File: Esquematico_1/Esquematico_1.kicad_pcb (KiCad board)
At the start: 6 copper layers, 40.7 x 40.7 mm, 93 parts, among them IC1 AP2112K-3.3TRG1, J1 Screw_Terminal_01x04, J2 Screw_Terminal_01x03, J3 Screw_Terminal_01x06, J4 Screw_Terminal_01x08, J5 SWD, J6 Screw_Terminal_01x04, J7 USB_C_Receptacle_USB2.0_16P, J8 Screw_Terminal_01x02, U1 ICM-42688-P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

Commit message: Update arreglo de errores
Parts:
- added J9: Screw_Terminal_01x01, TestPoint:TestPoint_Pad_2.5x2.5mm, B.Cu at (125.4, 95.5)
- J8: value Screw_Terminal_01x02 -> Screw_Terminal_01x01; footprint TerminalBlock:TerminalBlock_Xinya_XY308-2.54-2P_1x02_P2.54mm_Horizontal -> TestPoint:TestPoint_Pad_2.5x2.5mm
- moved J8 30.4 mm to (125.4, 100.4), turned to 180 degrees
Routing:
- net VCC: track 61.5 -> 79.3 mm, vias 2 -> 4

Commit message: Update pcb 0 errores
8========D
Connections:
- J7 pad A4: Net-(D3-A) -> (no net)
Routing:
- net USB_D+: track 0.00 -> 6.88 mm
- net USB_D-: track 0.00 -> 6.48 mm
- net Net-(J7-D+-PadA6): track 0.00 -> 5.48 mm
- net Net-(J7-D--PadA7): track 0.00 -> 4.97 mm
- net GND: track 58.6 -> 60.2 mm
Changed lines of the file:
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@@
 	(generator_version "9.0")
 	(general
-		(thickness 1.6)
+		(thickness 2.453)
 		(legacy_teardrops no)
 	)
@@
 			(layer "dielectric 1"
 				(type "prepreg")
-				(thickness 0.1)
-				(material "FR4")
-				(epsilon_r 4.5)
-				(loss_tangent 0.02)
+				(color "FR4 natural")
+				(thickness 0.994)
+				(material "3313 RC57% 4.2mil")
+				(epsilon_r 1)
+				(loss_tangent 0)
 			)
 			(layer "In1.Cu"
 				(type "copper")
-				(thickness 0.035)
+				(thickness 0.0152)
 			)
 			(layer "dielectric 2"
 				(type "core")
-				(thickness 0.535)
-				(material "FR4")
+				(thickness 0.55)
+				(material "0.55mm H/Hwithout copper")
 				(epsilon_r 4.5)
 				(loss_tangent 0.02)
@@
 			(layer "In2.Cu"
 				(type "copper")
-				(thickness 0.035)
+				(thickness 0.0152)
 			)
 			(layer "dielectric 3"
 				(type "prepreg")
-				(thickness 0.1)
-				(material "FR4")
+				(thickness 0.1088)
+				(material "2116 RC54% 4.9mil")
 				(epsilon_r 4.5)
 				(loss_tangent 0.02)
@@
 			(layer "In3.Cu"
 				(type "copper")
-				(thickness 0.035)
+				(thickness 0.0152)
 			)
 			(layer "dielectric 4"
 				(type "core")
-				(thickness 0.535)
-				(material "FR4")
+				(thickness 0.55)
+				(material "0.55mm H/Hwithout copper")
 				(epsilon_r 4.5)
 				(loss_tangent 0.02)
@@
 			(layer "In4.Cu"
 				(type "copper")
-				(thickness 0.035)
+				(thickness 0.0152)
 			)
 			(layer "dielectric 5"
 				(type "prepreg")
-				(thickness 0.1)
-				(material "FR4")
-				(epsilon_r 4.5)
-				(loss_tangent 0.02)
+				(color "FR4 natural")
+				(thickness 0.0994)
+				(material "3313 RC57% 4.2mil")
+				(epsilon_r 1)
+				(loss_tangent 0)
 			)
 			(layer "B.Cu"
@@
 			)
 			(copper_finish "None")
-			(dielectric_constraints no)
+			(dielectric_constraints yes)
 		)
 		(pad_to_mask_clearance 0)
@@
 			(size 0.6 1.15)
 			(layers "F.Cu" "F.Mask" "F.Paste")
-			(net 26 "Net-(D3-A)")
 			(pinfunction "VBUS")
 			(pintype "passive")
@@
 	)
 	(via
-		(at 114.6 90)
+		(at 115.1 91.44)
 		(size 0.45)
 		(drill 0.3)
@@
 	)
 	(segment
+		(start 114.5925 90.0075)
+		(end 113.23 90.0075)
+		(width 0.2)
+		(layer "B.Cu")
+		(net 4)
+	)
+	(segment
 		(start 104.9 99.7625)
 		(end 105.15 99.5125)
@@
 	)
 	(segment
-		(start 114.5925 90.0075)
-		(end 114.6 90)
+		(start 105.426 97.351)
+		(end 106.15 96.627)
 		(width 0.2)
 		(layer "B.Cu")
@@
 	)
 	(segment
-		(start 105.426 97.351)
-		(end 106.15 96.627)
+		(start 92.15 79.28)
+		(end 93.02 79.28)
 		(width 0.2)
 		(layer "B.Cu")
@@
 	)
 	(segment
-		(start 92.15 79.28)
-		(end 93.02 79.28)
+		(start 115.1 91.44)
+		(end 115.1 90.515)
 		(width 0.2)
 		(layer "B.Cu")
@@
 	)
 	(segment
-		(start 113.23 90.0075)
+		(start 115.1 90.515)
 		(end 114.5925 90.0075)
 		(width 0.2)
@@
 	)
 	(segment
+		(start 116.2783 90.1733)
+		(end 110.1108 90.1733)
+		(width 0.2)
+		(layer "F.Cu")
+		(net 14)
+	)
+	(segment
+		(start 116.4525 90.3475)
+		(end 116.2783 90.1733)
+		(width 0.2)
+		(layer "F.Cu")
+		(net 14)
+	)
+	(segment
+		(start 110.1108 90.1733)
+		(end 110.065 90.1275)
+		(width 0.2)
+		(layer "F.Cu")
+		(net 14)
+	)
+	(segment
 		(start 110.899 95.1275)
 		(end 110.065 95.1275)
@@
 	)
 	(segment
-		(start 117.114999 89.3975)
-		(end 117.366 89.146499)
-		(width 0.2)
-		(layer "F.Cu")
-		(net 18)
-	)
-	(segment
 		(start 95.38 79.42)
 		(end 95.38 79.5625)
@@
 	)
 	(segment
-		(start 116.4525 89.3975)
-		(end 117.114999 89.3975)
-		(width 0.2)
-		(layer "F.Cu")
-		(net 18)
-	)
-	(segment
 		(start 97 79.2)
 		(end 95.6 79.2)
@@
 	)
 	(segment
-		(start 117.366 86.4735)
+		(start 117.59 86.6975)
 		(end 116.6775 85.785)
 		(width 0.2)
@@
 	)
 	(segment
+		(start 116.4525 89.3975)
+		(end 117.114999 89.3975)
+		(width 0.2)
+		(layer "F.Cu")
+		(net 18)
+	)
+	(segment
 		(start 95.6 79.2)
 		(end 95.38 79.42)
@@
 	)
 	(segment
-		(start 117.366 89.146499)
-		(end 117.366 86.4735)
+		(start 117.114999 89.3975)
+		(end 117.59 88.922499)
+		(width 0.2)
+		(layer "F.Cu")
+		(net 18)
+	)
+	(segment
+		(start 117.59 88.922499)
+		(end 117.59 86.6975)
 		(width 0.2)
 		(layer "F.Cu")
@@
 	(segment
 		(start 121.265 87.4375)
-		(end 122.156008 87.4375)
+		(end 122.6025 87.4375)
 		(width 0.2)
 		(layer "F.Cu")
@@
 	)
 	(segment
-		(start 122.156008 87.4375)
-		(end 123.141 86.452508)
+		(start 123.27 81.3075)
+		(end 122.84 80.8775)
 		(width 0.2)
 		(layer "F.Cu")
@@
 	)
 	(segment
-		(start 123.141 86.452508)
-		(end 123.141 81.1785)
+		(start 123.27 86.77)
+		(end 123.27 81.3075)
 		(width 0.2)
 		(layer "F.Cu")
@@
 	)
 	(segment
-		(start 123.141 81.1785)
-		(end 122.84 80.8775)
+		(start 122.6025 87.4375)
+		(end 123.27 86.77)
 		(width 0.2)
 		(layer "F.Cu")
@@
 	)
 	(segment
+		(start 114.224098 89.6275)
+		(end 110.065 89.6275)
+		(width 0.2)
+		(layer "F.Cu")
+		(net 53)
+	)
+	(segment
+		(start 116.4525 88.4475)
+		(end 115.404098 88.4475)
+		(width 0.2)
+		(layer "F.Cu")
+		(net 53)
+	)
+	(segment
+		(start 115.404098 88.4475)
+		(end 114.224098 89.6275)
+		(width 0.2)
+		(layer "F.Cu")
+		(net 53)
+	)
+	(segment
 		(start 110.065 90.6275)
 		(end 107.4275 90.6275)
@@
 	)
 	(segment
+		(start 119.95 89.4775)
+		(end 119.95 90.2)
+		(width 0.2)
+		(layer "F.Cu")
+		(net 62)
+	)
+	(segment
+		(start 120.49 88.9375)
+		(end 119.95 89.4775)
+		(width 0.2)
+		(layer "F.Cu")
+		(net 62)
+	)
+	(segment
+		(start 121.265 89.9375)
+		(end 120.2125 89.9375)
+		(width 0.2)
+		(layer "F.Cu")
+		(net 62)
+	)
+	(segment
+		(start 119.8025 90.3475)
+		(end 118.7275 90.3475)
+		(width 0.2)
+		(layer "F.Cu")
+		(net 62)
+	)
+	(segment
+		(start 121.265 88.9375)
+		(end 120.49 88.9375)
+		(width 0.2)
+		(layer "F.Cu")
+		(net 62)
+	)
+	(segment
+		(start 120.2125 89.9375)
+		(end 119.95 90.2)
+		(width 0.2)
+		(layer "F.Cu")
+		(net 62)
+	)
+	(segment
+		(start 119.95 90.2)
+		(end 119.8025 90.3475)
+		(width 0.2)
+		(layer "F.Cu")
+		(net 62)
+	)
+	(segment
 		(start 106.65 84.87)
 		(end 106.65 86.1925)
@@
 	)
 	(segment
+		(start 122.1825 89.4375)
+		(end 122.34 89.28)
+		(width 0.2)
+		(layer "F.Cu")
+		(net 86)
+	)
+	(segment
+		(start 122.34 88.64)
+		(end 122.1375 88.4375)
+		(width 0.2)
+		(layer "F.Cu")
+		(net 86)
+	)
+	(segment
+		(start 118.7375 88.4375)
+		(end 118.7275 88.4475)
+		(width 0.2)
+		(layer "F.Cu")
+		(net 86)
+	)
+	(segment
+		(start 121.265 88.4375)
+		(end 118.7375 88.4375)
+		(width 0.2)
+		(layer "F.Cu")
+		(net 86)
+	)
+	(segment
+		(start 122.34 89.28)
+		(end 122.34 88.64)
+		(width 0.2)
+		(layer "F.Cu")
+		(net 86)
+	)
+	(segment
+		(start 121.265 89.4375)
+		(end 122.1825 89.4375)
+		(width 0.2)
+		(layer "F.Cu")
+		(net 86)
+	)
+	(segment
+		(start 122.1375 88.4375)
+		(end 121.265 88.4375)
+		(width 0.2)
+		(layer "F.Cu")
+		(net 86)
+	)
+	(segment

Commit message: Pequeños retoques de los nombres
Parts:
- renumbered SwBoot1 to Boot, F5 to GPS, SwReset1 to Reset
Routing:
- net GND: track 60.2 -> 62.5 mm, vias 33 -> 35
- net SDIO_D1: track 6.63 -> 6.06 mm

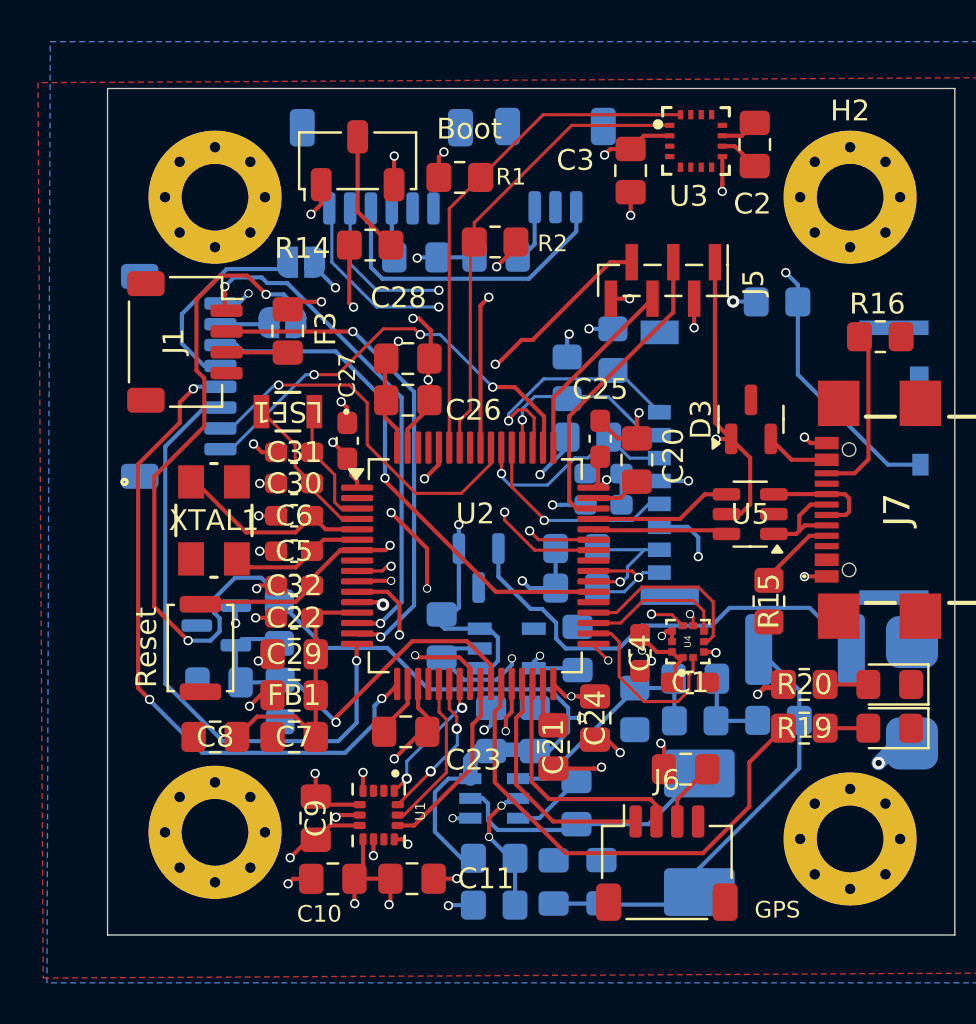
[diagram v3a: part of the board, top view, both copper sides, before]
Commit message: Add 3d model pa
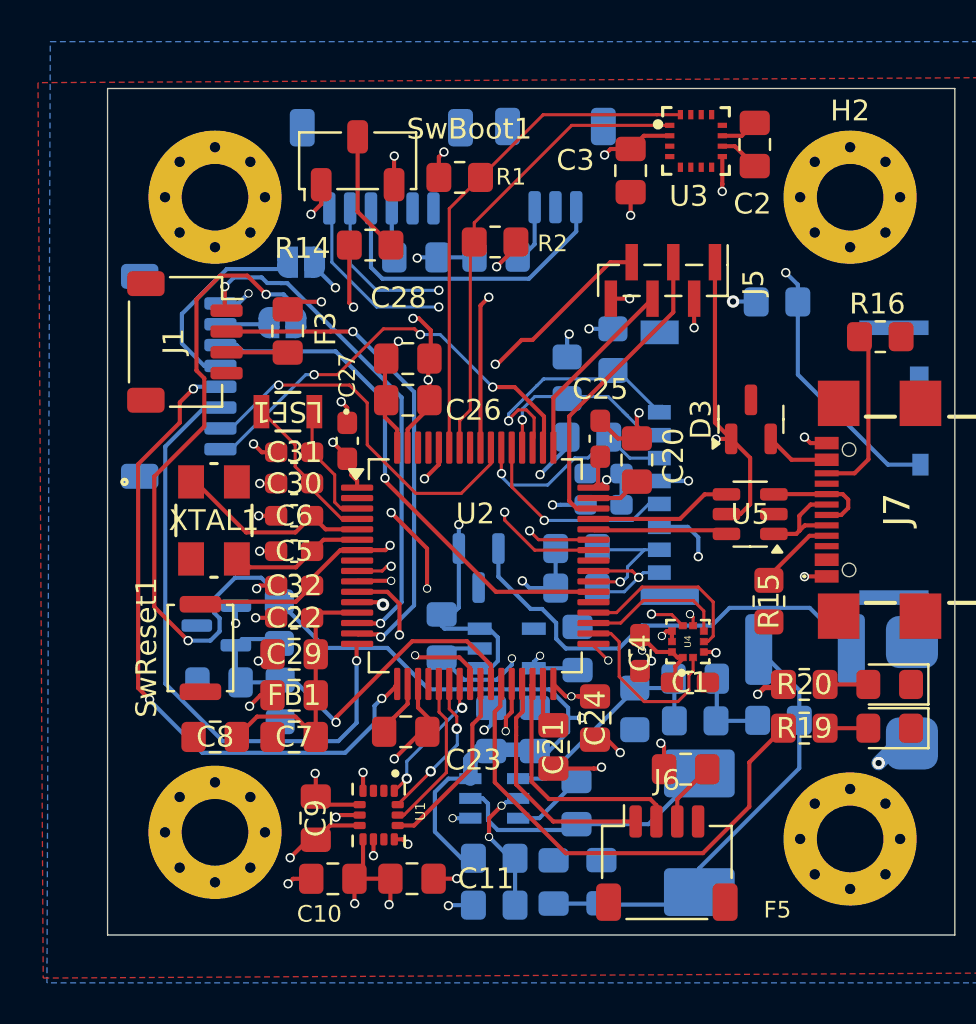
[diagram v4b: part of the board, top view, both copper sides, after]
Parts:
- renumbered GPS to F5, Boot to SwBoot1, Reset to SwReset1
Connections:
- J7 pad A4: (no net) -> Net-(D3-A)
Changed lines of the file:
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@@
 		(descr "Capacitor SMD 0805 (2012 Metric), square (rectangular) end terminal, IPC-7351 nominal with elongated pad for handsoldering. (Body size source: IPC-SM-782 page 76, https://www.pcb-3d.com/wordpress/wp-content/uploads/ipc-sm-782a_amendment_1_and_2.pdf, https://docs.google.com/spreadsheets/d/1BsfQQcO9C6DZCsRaXUlFlo91Tg2WpOkGARC1WS5S8t0/edit?usp=sharing), generated with kicad-footprint-generator")
 		(tags "capacitor handsolder")
-		(property "Reference" "GPS"
+		(property "Reference" "F5"
 			(at -4.4075 -6.7525 0)
 			(layer "F.SilkS")
@@
 				(font
 					(size 0.48 0.48)
-					(thickness 0.15)
+					(thickness 0.12)
 				)
 			)
@@
 				(font
 					(size 0.48 0.48)
-					(thickness 0.15)
+					(thickness 0.12)
 				)
 			)
@@
 		)
 		(embedded_fonts no)
+		(model "${KIPRJMOD}/Footprints/ICM_42688_P/ICM-42688-P.step"
+			(offset
+				(xyz 0 0 0)
+			)
+			(scale
+				(xyz 1 1 1)
+			)
+			(rotate
+				(xyz -90 -0 -0)
+			)
+		)
 	)
 	(footprint "Resistor_SMD:R_0805_2012Metric_Pad1.20x1.40mm_HandSolder"
@@
 		)
 		(embedded_fonts no)
+		(model "${KIPRJMOD}/Footprints/BMP388/BMP388.step"
+			(offset
+				(xyz 0 0 0)
+			)
+			(scale
+				(xyz 1 1 1)
+			)
+			(rotate
+				(xyz -90 -0 90)
+			)
+		)
 	)
 	(footprint "Button_Switch_SMD:Nidec_Copal_CAS-120A"
@@
 		(descr "Slide Switch, SMD, Nidec CAS series, https://www.nidec-components.com/e/catalog/switch/cas.pdf")
 		(tags "SMD slide switch Nidec CAS 120A ")
-		(property "Reference" "Boot"
+		(property "Reference" "SwBoot1"
 			(at 1.5275 5.36 0)
 			(unlocked yes)
@@
 			(size 0.6 1.15)
 			(layers "F.Cu" "F.Mask" "F.Paste")
+			(net 26 "Net-(D3-A)")
 			(pinfunction "VBUS")
 			(pintype "passive")
@@
 		)
 		(embedded_fonts no)
+		(model "${KIPRJMOD}/Footprints/LIB_USB4940-00-A/ul_2295018-2/c-2295018-2-b-3d.stp"
+			(offset
+				(xyz 0 -4 1.3)
+			)
+			(scale
+				(xyz 1 1 1)
+			)
+			(rotate
+				(xyz -90 -0 -0)
+			)
+		)
 	)
 	(footprint "Capacitor_SMD:C_0805_2012Metric_Pad1.18x1.45mm_HandSolder"
@@
 		(descr "http://www.alps.com/prod/info/E/HTML/Tact/SurfaceMount/SKRK/SKRKAHE020.html")
 		(tags "SMD SMT button")
-		(property "Reference" "Reset"
+		(property "Reference" "SwReset1"
 			(at 0.0275 -2.59 90)
 			(layer "F.SilkS")
@@
 		)
 		(embedded_fonts no)
+		(model "${KIPRJMOD}/Footprints/MOLEX 5033981892/ul_5033981892/5033981892.stp"
+			(offset
+				(xyz -136 -16 154.4)
+			)
+			(scale
+				(xyz 1 1 1)
+			)
+			(rotate
+				(xyz -0 -180 -180)
+			)
+		)
 	)
 	(footprint "Capacitor_SMD:C_0805_2012Metric_Pad1.18x1.45mm_HandSolder"
@@
 	)
 	(segment
-		(start 122.1825 89.4375)
-		(end 122.34 89.28)
+		(start 122.3 88.7)
+		(end 122.0375 88.4375)
 		(width 0.2)
 		(layer "F.Cu")
@@
 	)
 	(segment
-		(start 122.34 88.64)
-		(end 122.1375 88.4375)
+		(start 118.7375 88.4375)
+		(end 118.7275 88.4475)
 		(width 0.2)
 		(layer "F.Cu")
@@
 	)
 	(segment
-		(start 118.7375 88.4375)
-		(end 118.7275 88.4475)
+		(start 121.265 89.4375)
+		(end 121.9625 89.4375)
 		(width 0.2)
 		(layer "F.Cu")
@@
 	)
 	(segment
-		(start 121.265 88.4375)
-		(end 118.7375 88.4375)
+		(start 121.9625 89.4375)
+		(end 122.3 89.1)
 		(width 0.2)
 		(layer "F.Cu")
@@
 	)
 	(segment
-		(start 122.34 89.28)
-		(end 122.34 88.64)
+		(start 122.3 89.1)
+		(end 122.3 88.7)
 		(width 0.2)
 		(layer "F.Cu")
@@
 	)
 	(segment
-		(start 121.265 89.4375)
-		(end 122.1825 89.4375)
+		(start 121.265 88.4375)
+		(end 118.7375 88.4375)
 		(width 0.2)
 		(layer "F.Cu")
@@
 	)
 	(segment
-		(start 122.1375 88.4375)
+		(start 122.0375 88.4375)
 		(end 121.265 88.4375)
 		(width 0.2)

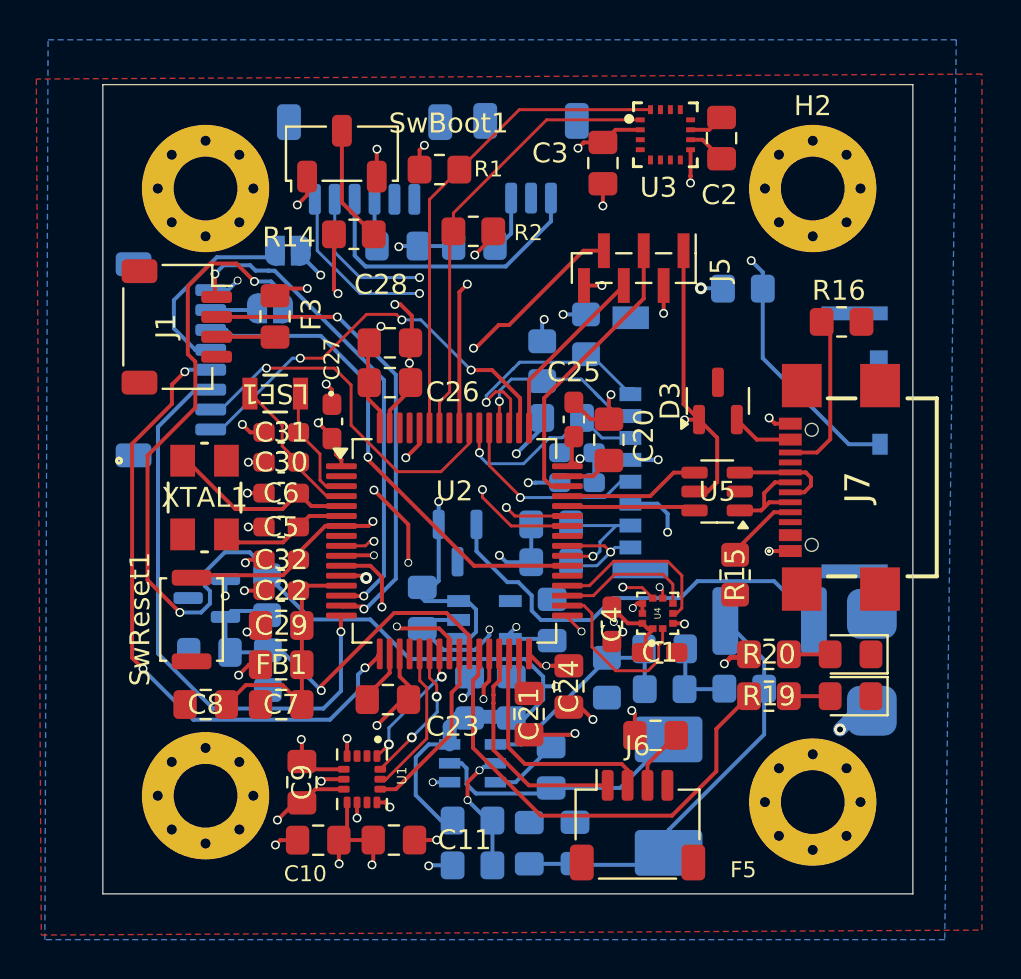
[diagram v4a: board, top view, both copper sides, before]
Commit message: Cambio de la SD, re ruteo del ESC para mayor fiabilidad, correción en el clearence
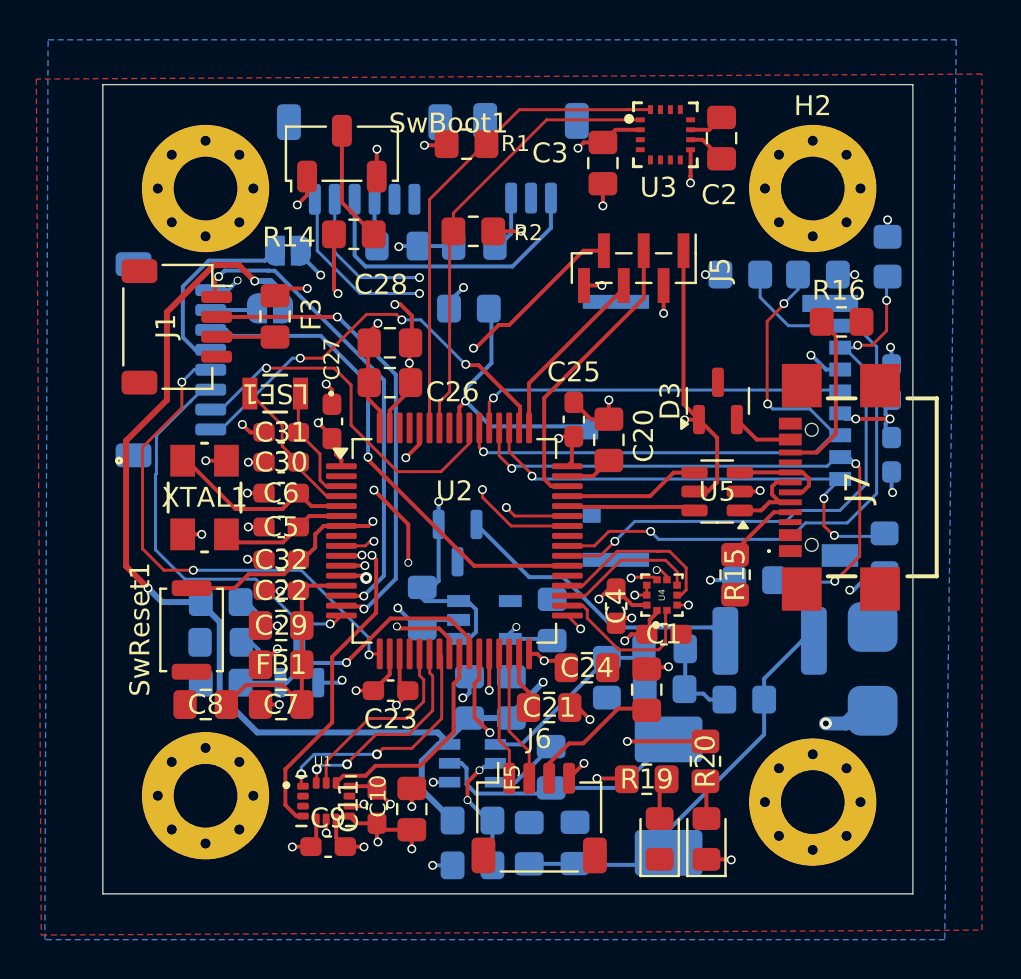
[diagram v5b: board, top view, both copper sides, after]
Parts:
- C11, C23, C9: footprint Capacitor_SMD:C_0805_2012Metric_Pad1.18x1.45mm_HandSolder -> Capacitor_SMD:C_0603_1608Metric_Pad1.08x0.95mm_HandSolder
- moved R7 21.6 mm to (126.2, 77.6), turned to -90 degrees
- moved R4 18.6 mm to (126.0, 92.5), turned to 90 degrees
- moved R8 17.3 mm to (118.8, 78.5)
- moved C34 16.6 mm to (126.3, 83.9), turned to -90 degrees
- moved C35 15.8 mm to (126.3, 87.5), turned to 90 degrees
- moved R5 15.3 mm to (119.5, 93.8), turned to 0 degrees
- moved R6 14.7 mm to (122.7, 78.5), turned to 180 degrees
- moved R3 13.8 mm to (105.1, 80.2)
- moved D8 12.0 mm to (114.7, 106.8), turned to 90 degrees
- moved D7 11.8 mm to (117.0, 106.8), turned to 90 degrees
- moved R19 7.42 mm to (114.0, 103.8)
- moved R20 6.25 mm to (117.0, 103.0), turned to -90 degrees
- moved D1 5.71 mm to (96.6, 98.1), turned to 90 degrees
- moved J6 4.95 mm to (108.7, 105.8)
- moved C10 4.95 mm to (102.2, 105.3), turned to 90 degrees
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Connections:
- J7 pad A4: Net-(D3-A) -> (no net)
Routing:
- net SDIO_D1: track 6.06 -> 32.4 mm
- net SDIO_D0: track 6.38 -> 29.4 mm, vias 1 -> 3
- net CardDetect: track 35.0 -> 13.6 mm, vias 2 -> 1
- net SDIO_CMD: track 10.5 -> 31.0 mm, vias 1 -> 3
- net SDIO_D3: track 9.79 -> 29.6 mm, vias 1 -> 3
- net SDIO_D2: track 12.2 -> 24.5 mm, vias 1 -> 3
- net /MCU/LRed: track 23.9 -> 12.2 mm, vias 0 -> 2
- net SDIO_CLK: track 10.0 -> 19.2 mm
- net ESC3: track 29.3 -> 20.5 mm
- net ESC4: track 32.5 -> 25.5 mm
- net Net-(D4-A): track 21.8 -> 15.7 mm
- net /MCU/LGreen: track 19.9 -> 13.8 mm
- net VCC: track 79.3 -> 73.2 mm
- net +3V3: track 63.0 -> 57.2 mm, vias 24 -> 27
- net MOSI_IMU: track 6.59 -> 12.3 mm
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
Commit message: Cambios menores
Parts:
- moved C5 0.20 mm to (95.7, 91.4), turned to 0 degrees
- moved C6 0.05 mm to (95.7, 89.4), turned to 0 degrees
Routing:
- net /MCU/HSE_IN: track 9.60 -> 8.92 mm
- net GND: track 57.9 -> 57.6 mm, vias 39 -> 38

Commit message: Correcciones menores
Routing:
- net GND: track 57.6 -> 55.6 mm, vias 38 -> 36
- net INT1_IMU: vias 2 -> 1

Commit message: Cambios de Diodos
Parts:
- added D2: D_ST, Diode_SMD:D_SOD-323_HandSoldering, F.Cu at (116.1, 81.6)
- D1, D3, D4: footprint Package_TO_SOT_SMD:SOT-23 -> Diode_SMD:D_SOD-323_HandSoldering
- moved D4 1.71 mm to (106.0, 92.8), turned to 0 degrees
- moved D3 0.98 mm to (117.4, 85.8), turned to 0 degrees
- moved H1 0.32 mm to (122.4, 104.7)
- moved D1 0.29 mm to (96.6, 98.3), turned to -90 degrees
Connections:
- J5 pad 2: +3V3 -> Net-(D2-A)
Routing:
- net GND: track 55.6 -> 60.0 mm, vias 36 -> 69
- net LDO_USB: track 61.6 -> 65.1 mm, vias 4 -> 5
- net Net-(D2-A): track 0.00 -> 2.54 mm
- net Net-(D4-A): track 15.7 -> 13.2 mm
- net +3V3: track 57.2 -> 58.3 mm, vias 27 -> 28
- net Bat_Med_FC: track 20.3 -> 20.8 mm
- net SWD_NRST: vias 2 -> 3
- net (no net): vias 0 -> 1
